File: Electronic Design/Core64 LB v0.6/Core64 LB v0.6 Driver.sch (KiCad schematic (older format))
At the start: 68 parts, among them J1 SSW-116-22-F-S-VS‎, J13 Core Cur. Mon., J2 SSW-116-22-F-S-VS‎, Q10 MMBT4401LT1G, Q11 MMBT4403LT1G, Q12 MMBT4401LT1G, Q13 MMBT4403LT1G, Q14 MMBT4401LT1G, Q15 MMBT4403LT1G, Q16 MMBT4401LT1G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

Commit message: APPLY LOGIC BOARD V0.5 FIXES NEEDED TO BE V0.6 U1 silk screen should be placed by pin 1 not pin 7 Check J1 and J2 labels so J1 is on the left, like it is for the Core Board Remove Header for old LED Matrix, since is no longer needed and it is in the way. RTC Notes on schematic, must add THREE things, typo change from TWO. Below JP5 Teensy Charge Enable is a rogue "+" on the silk screen Left of R56 is a dead-end trace stub. Doesn't hurt anything but it's not right. 6.8 Ohm Core Current Limit Resistors can move to 5%. JP1/2 for OLED should be JP1/2 on the OLED silk screen, not JP3/4 Silk screen, left header row, swap SEN1 and SEN2 text so they match to S1 and S2 correctly on the inner perimeter. Move to larger logo and other text on the backside Update silk screen for all boards with P/Ns, bare board. Move top row of TFT LCD support down 0.55mm. Add 470 resistor to gate of core array enable to limit current. Change I2C pull-up resistors from 2.2K to 1.2K 20% (E12 series is most common, and values overlap) Remove two dead-end GND (BAT-) traces between/below Teensy 25/26, and over to QWIIC. Add I2C series resistors 68 Ohm at output of Teensy. Move the 470uF LED 5V0 capacitor, down to be between 5V0 Cur Mon and Teensy Charge enable jumpers, out of the way of the batteries. New stylus position is on left, so the 3V3 capacitor needs to move in a few mm to allow it to pass through. Provide thru-holes for alternate 3.3V and 5V bulk capacitor options. Propagation through sense logic chips was 200ns, reduce PU to 1K2 and remove inline 10Ks. Now 50ns. Voltage divider and other resistors, consolidated to 10K resistors. Keep the two 10K resistors on the 5V0 MON. Add a SJ in series to isolate from Hall Switches. Replace the inline 10K resistors in the all optional Voltage Monitoring lines with closed SJs instead. Clean-up all the horz/vert traces left from removing LED drive header and relocating the driver and 5V0 cap Part substitutions Data sheet updates
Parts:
- added J10, J15: Conn_01x01_Male, Connector_PinHeader_2.54mm:PinHeader_1x01_P2.54mm_Vertical_No_Registration, symbol Connector:Conn_01x01_Male
- added R59: 470, Resistor_SMD:R_0805_2012Metric, symbol Device:R
- D1, D11, D3, D5, D7, D9: Description (none) -> DIODE ARRAY SCHOTTKY 30V; MPN (none) -> BAT54AW-7-F; Manufacturer_Name (none) -> Diodes Inc.
- D10, D12, D2, D4, D6, D8: Description (none) -> DIODE ARRAY SCHOTTKY 30V; MPN (none) -> BAT54CW-7-F; Manufacturer_Name (none) -> Diodes Inc.
- Q10, Q12, Q14, Q16, Q18, Q20, Q22, Q3, Q5, Q7: MPN(Secondary) (none) -> MMBT4401-7-F; Manufacturer(Secondary) (none) -> Diodes Inc.; Manufacturer_Name (none) -> Onsemi
- Q11, Q13, Q15, Q17, Q19, Q2, Q21, Q4, Q6, Q9: MPN(Secondary) (none) -> MMBT4403-7-F; Manufacturer(Secondary) (none) -> Diodes Inc.; Manufacturer_Name (none) -> Onsemi
- Q8: value Q_NMOS_DGS_NVTR4503NT1G -> NVTR4503NT1G_NMOS_GSD; Description (none) -> MOSFET N-CHNL GSD LOW RDS(ON); MPN (none) -> NVTR4503NT1G; MPN(Secondary) (none) -> IRLML2030TRPBF; Manufacturer(Secondary) (none) -> Infineon Technologies; Manufacturer_Name (none) -> Onsemi
- R21, R26, R27, R28, R31, R38: value 6R8-1% -> 6R8-5%
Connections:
- net GND: now also J15.1 (Pin_1)
- net SENSE1: now also J1.10 (Pin_10); no longer J1.9 (Pin_9)
- net SENSE2: now also J1.9 (Pin_9); no longer J1.10 (Pin_10)
- net VMEM: now also J10.1 (Pin_1)
- net WRITE_ENABLE: now also R59.2; no longer Q8.1 (G)
- new net: Q8.1 (G), R59.1
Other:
- note added: "+"
- note added: "DNI"
- note added: "GND"
- note added: "Optional: Thru hole radial lead Cap.\n2.5mm lead spacing, 6.3mm dia, 12.5mm tall"
- moved on the sheet: C1

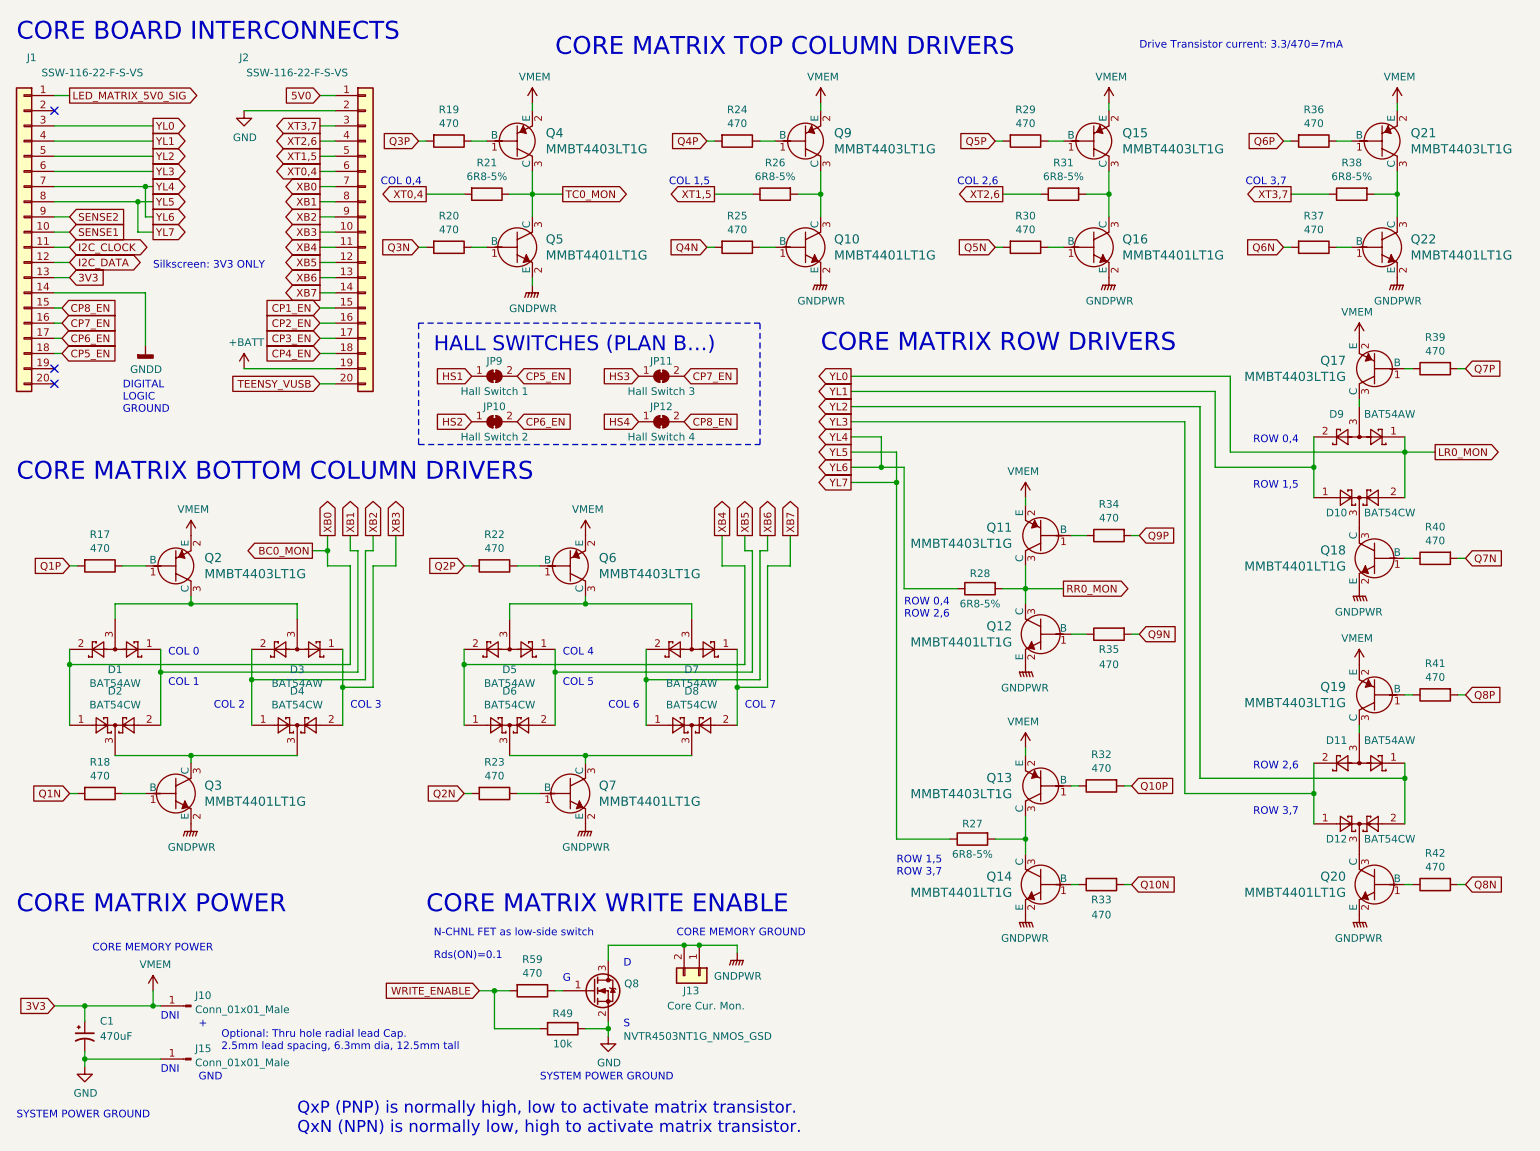
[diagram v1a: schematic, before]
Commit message: Revise LB V0.6, part substitutions, data sheet updates, clean up Ref. Des. to be in order and easier to find on the board in groups
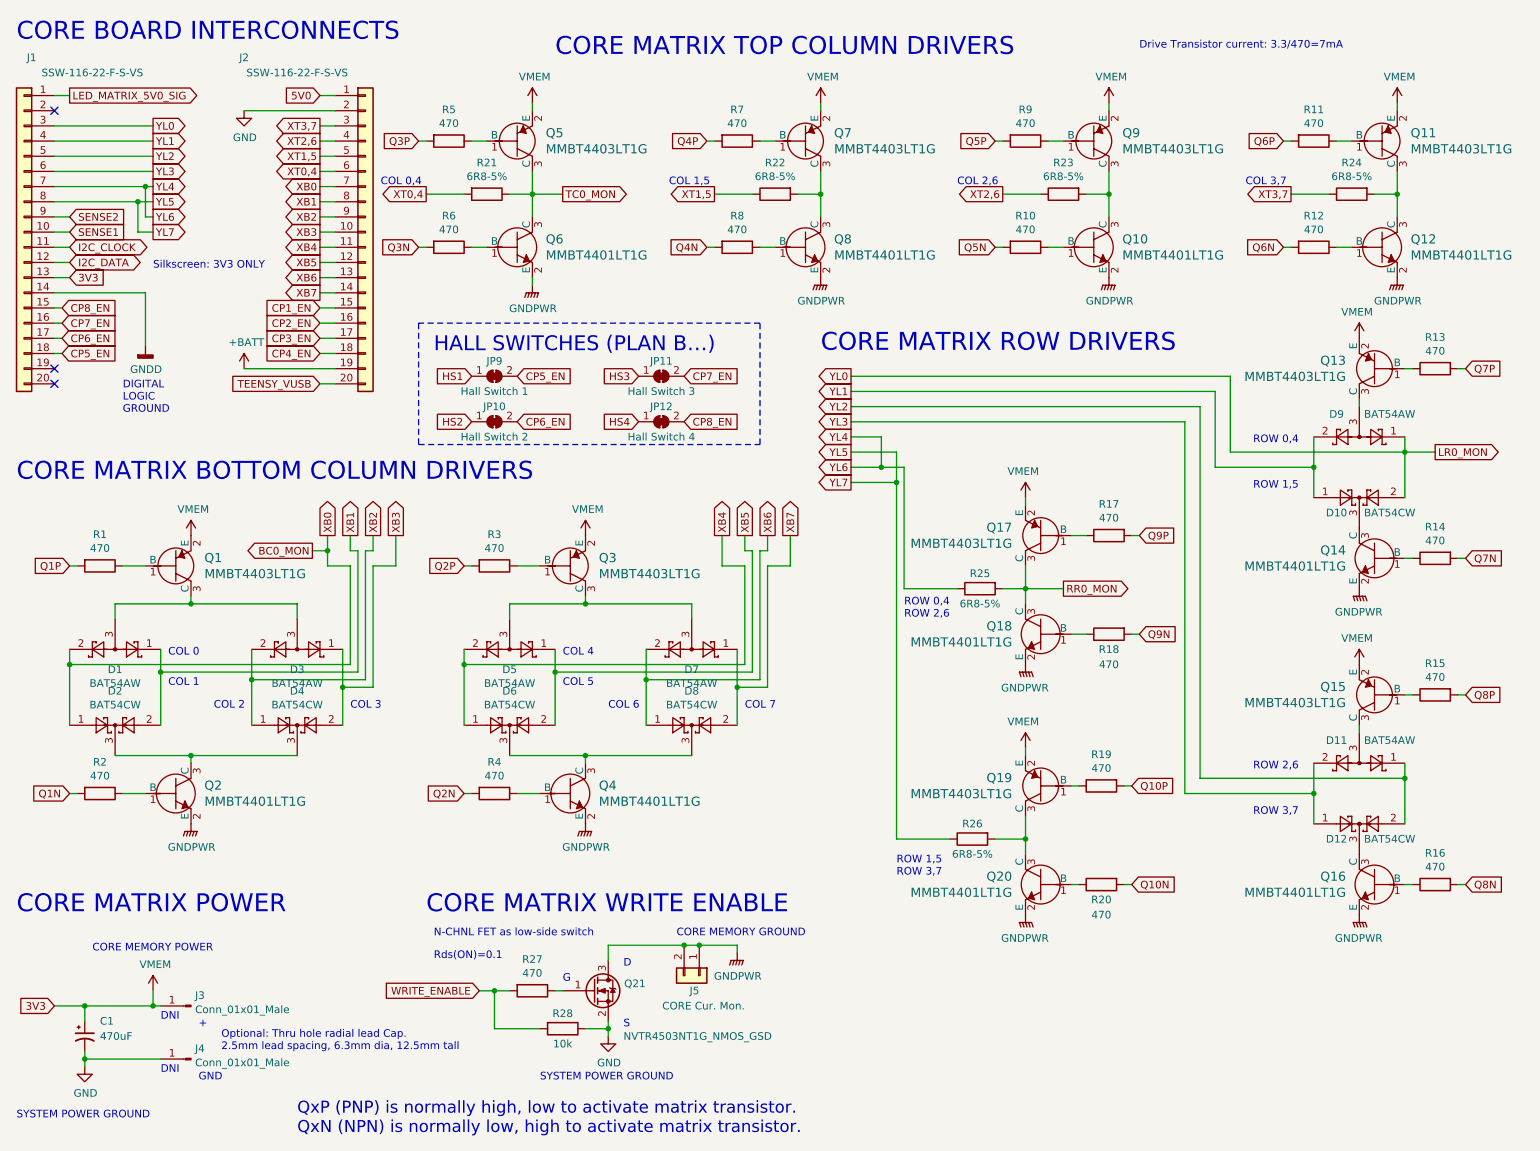
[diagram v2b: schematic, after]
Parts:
- C1: Description (none) -> CAP ALUM 470UF 20% 10V SMD; Insert? (none) -> Yes; MPN(Secondary) (none) -> 6.3SEV330M6.3X8; Manufacturer(Secondary) (none) -> Rubycon; Value_Modifier (none) -> 330UF 20% 6.3V
- D1, D10, D11, D12, D2, D3, D4, D5, D6, D7, D8, D9: Insert? (none) -> Yes
- J1, J2, JP10, JP11, JP12, JP9: Insert? (none) -> No
- J3: renamed from J10; Insert? (none) -> No
- J4: renamed from J15; Insert? (none) -> No
- J5: renamed from J13; value Core Cur. Mon. -> CORE Cur. Mon.; Insert? (none) -> No
- Q1: renamed from Q2; Insert? (none) -> Yes
- Q10: renamed from Q16; Insert? (none) -> Yes
- Q11: renamed from Q21; Insert? (none) -> Yes
- Q12: renamed from Q22; Insert? (none) -> Yes
- Q13: renamed from Q17; Insert? (none) -> Yes
- Q14: renamed from Q18; Insert? (none) -> Yes
- Q15: renamed from Q19; Insert? (none) -> Yes
- Q16: renamed from Q20; Insert? (none) -> Yes
- Q17: renamed from Q11; Insert? (none) -> Yes
- Q18: renamed from Q12; Insert? (none) -> Yes
- Q19: renamed from Q13; Insert? (none) -> Yes
- Q2: renamed from Q3; Insert? (none) -> Yes
- Q20: renamed from Q14; Insert? (none) -> Yes
- Q21: renamed from Q8; Insert? (none) -> Yes
- Q3: renamed from Q6; Insert? (none) -> Yes
- Q4: renamed from Q7; Insert? (none) -> Yes
- Q5: renamed from Q4; Insert? (none) -> Yes
- Q6: renamed from Q5; Insert? (none) -> Yes
- Q7: renamed from Q9; Insert? (none) -> Yes
- Q8: renamed from Q10; Insert? (none) -> Yes
- Q9: renamed from Q15; Insert? (none) -> Yes
- R1: renamed from R17; Description (none) -> RES 470 OHM; Insert? (none) -> Yes; Value_Modifier (none) -> 10%
- R10: renamed from R30; Description (none) -> RES 470 OHM; Insert? (none) -> Yes; Value_Modifier (none) -> 10%
- R11: renamed from R36; Description (none) -> RES 470 OHM; Insert? (none) -> Yes; Value_Modifier (none) -> 10%
- R12: renamed from R37; Description (none) -> RES 470 OHM; Insert? (none) -> Yes; Value_Modifier (none) -> 10%
- R13: renamed from R39; Description (none) -> RES 470 OHM; Insert? (none) -> Yes; Value_Modifier (none) -> 10%
- R14: renamed from R40; Description (none) -> RES 470 OHM; Insert? (none) -> Yes; Value_Modifier (none) -> 10%
- R15: renamed from R41; Description (none) -> RES 470 OHM; Insert? (none) -> Yes; Value_Modifier (none) -> 10%
- R16: renamed from R42; Description (none) -> RES 470 OHM; Insert? (none) -> Yes; Value_Modifier (none) -> 10%
- R17: renamed from R34; Description (none) -> RES 470 OHM; Insert? (none) -> Yes; Value_Modifier (none) -> 10%
- R18: renamed from R35; Description (none) -> RES 470 OHM; Insert? (none) -> Yes; Value_Modifier (none) -> 10%
- R19: renamed from R32; Description (none) -> RES 470 OHM; Insert? (none) -> Yes; Value_Modifier (none) -> 10%
- R2: renamed from R18; Description (none) -> RES 470 OHM; Insert? (none) -> Yes; Value_Modifier (none) -> 10%
- R20: renamed from R33; Description (none) -> RES 470 OHM; Insert? (none) -> Yes; Value_Modifier (none) -> 10%
- R21: Description (none) -> RES 6.8 OHM 1/8W 0805; Insert? (none) -> Yes; Value_Modifier (none) -> 5%
- R22: renamed from R26; Description (none) -> RES 6.8 OHM 1/8W 0805; Insert? (none) -> Yes; Value_Modifier (none) -> 5%
- R23: renamed from R31; Description (none) -> RES 6.8 OHM 1/8W 0805; Insert? (none) -> Yes; Value_Modifier (none) -> 5%
- R24: renamed from R38; Description (none) -> RES 6.8 OHM 1/8W 0805; Insert? (none) -> Yes; Value_Modifier (none) -> 5%
- R25: renamed from R28; Description (none) -> RES 6.8 OHM 1/8W 0805; Insert? (none) -> Yes; Value_Modifier (none) -> 5%
- R26: renamed from R27; Description (none) -> RES 6.8 OHM 1/8W 0805; Insert? (none) -> Yes; Value_Modifier (none) -> 5%
- R27: renamed from R59; Description (none) -> RES 470 OHM; Insert? (none) -> Yes; Value_Modifier (none) -> 10%
- R28: renamed from R49; Description (none) -> RES 10K OHM; Insert? (none) -> Yes; Value_Modifier (none) -> 20%
- R3: renamed from R22; Description (none) -> RES 470 OHM; Insert? (none) -> Yes; Value_Modifier (none) -> 10%
- R4: renamed from R23; Description (none) -> RES 470 OHM; Insert? (none) -> Yes; Value_Modifier (none) -> 10%
- R5: renamed from R19; Description (none) -> RES 470 OHM; Insert? (none) -> Yes; Value_Modifier (none) -> 10%
- R6: renamed from R20; Description (none) -> RES 470 OHM; Insert? (none) -> Yes; Value_Modifier (none) -> 10%
- R7: renamed from R24; Description (none) -> RES 470 OHM; Insert? (none) -> Yes; Value_Modifier (none) -> 10%
- R8: renamed from R25; Description (none) -> RES 470 OHM; Insert? (none) -> Yes; Value_Modifier (none) -> 10%
- R9: renamed from R29; Description (none) -> RES 470 OHM; Insert? (none) -> Yes; Value_Modifier (none) -> 10%

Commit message: Refine LB v0.6 layout, KiCAD BOM updates, review schematic and PCB for release
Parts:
- renumbered JP9 to JP1, JP10 to JP2, JP11 to JP3, JP12 to JP4
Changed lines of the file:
@@
 Sheet 5 5
 Title "Core 64 - Core Matrix Driver"
-Date "2021-11-08"
+Date "2021-11-09"
 Rev "0.6"
 Comp "Concept and design by Andy Geppert @ www.MachineIdeas.com"
 Comment1 "Visit www.Core64.io for information on assembly and optional features."
-Comment2 "WIP"
+Comment2 "As released"
 Comment3 ""
 Comment4 "All non-polarized capacitors are X7R or X5R ceramic unless otherwise noted."
@@
 CP8_EN
 $Comp
-L Jumper:SolderJumper_2_Bridged JP12
+L Jumper:SolderJumper_2_Bridged JP4
 U 1 1 60397BD0
 P 4800 3250
-F 0 "JP12" H 4800 3150 50  0000 C CNN
+F 0 "JP4" H 4800 3150 50  0000 C CNN
 F 1 "Hall Switch 4" H 4800 3350 50  0000 C CNN
 F 2 "Jumper:SolderJumper-2_P1.3mm_Bridged_RoundedPad1.0x1.5mm" H 4800 3250 50  0001 C CNN
@@
 $EndComp
 $Comp
-L Jumper:SolderJumper_2_Bridged JP11
+L Jumper:SolderJumper_2_Bridged JP3
 U 1 1 603B8476
 P 4800 2950
-F 0 "JP11" H 4800 2850 50  0000 C CNN
+F 0 "JP3" H 4800 2850 50  0000 C CNN
 F 1 "Hall Switch 3" H 4800 3050 50  0000 C CNN
 F 2 "Jumper:SolderJumper-2_P1.3mm_Bridged_RoundedPad1.0x1.5mm" H 4800 2950 50  0001 C CNN
@@
 $EndComp
 $Comp
-L Jumper:SolderJumper_2_Bridged JP9
+L Jumper:SolderJumper_2_Bridged JP1
 U 1 1 6040AAB4
 P 3700 2950
-F 0 "JP9" H 3700 2850 50  0000 C CNN
+F 0 "JP1" H 3700 2850 50  0000 C CNN
 F 1 "Hall Switch 1" H 3700 3050 50  0000 C CNN
 F 2 "Jumper:SolderJumper-2_P1.3mm_Bridged_RoundedPad1.0x1.5mm" H 3700 2950 50  0001 C CNN
@@
 $EndComp
 $Comp
-L Jumper:SolderJumper_2_Bridged JP10
+L Jumper:SolderJumper_2_Bridged JP2
 U 1 1 6041B0A8
 P 3700 3250
-F 0 "JP10" H 3700 3150 50  0000 C CNN
+F 0 "JP2" H 3700 3150 50  0000 C CNN
 F 1 "Hall Switch 2" H 3700 3350 50  0000 C CNN
 F 2 "Jumper:SolderJumper-2_P1.3mm_Bridged_RoundedPad1.0x1.5mm" H 3700 3250 50  0001 C CNN

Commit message: LB V0.6 Released for production
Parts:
- C1: MPN (none) -> EEE-FTA471XAL; Manufacturer_Name (none) -> Panasonic
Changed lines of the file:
@@
 F 8 "Rubycon" H 1000 7300 50  0001 C CNN "Manufacturer(Secondary)"
 F 9 "330UF 20% 6.3V" H 1000 7300 50  0001 C CNN "Value_Modifier"
+F 10 "EEE-FTA471XAL" H 1000 7300 50  0001 C CNN "MPN"
+F 11 "Panasonic" H 1000 7300 50  0001 C CNN "Manufacturer_Name"
 	1    1000 7300
 	1    0    0    -1
